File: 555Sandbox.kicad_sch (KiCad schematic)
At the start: 18 parts, among them J1 VIN, J2 Piezo, Q1 2N7000, SW1 RESET, U1 NE555P

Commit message: feat: update with separate freq and period adjustment
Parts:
- removed Q1: 2N7000, Package_TO_SOT_THT:TO-92_Inline, symbol Transistor_FET:2N7000
- added R7: 4K7, Resistor_THT:R_Axial_DIN0207_L6.3mm_D2.5mm_P7.62mm_Horizontal, symbol Device:R
- R6: value 10K -> 4K7
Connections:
- net GND: now also J2.1 (Pin_1), R5.2
- net OUT: now also D1.2 (A), J2.2 (Pin_2), U1.3 (Q); no longer J2.1 (Pin_1), R5.2
- net TRIG: now also RV1.2; no longer C3.1, RV1.3
- net VCC: now also R7.1; no longer D1.2 (A), J2.2 (Pin_2), R6.1
- net DIS: now reaches D12.2 (A), D13.1 (K)
- net DIS: now also U1.7 (DIS), R7.2; no longer U1.3 (Q)
- net VCAP: now reaches RV2.1, RV2.2
- net VCAP: now also C3.1; no longer D13.2 (A)
- net at D12.1 (K), RV1.1: no longer RV1.2
- net OSC_OUT: no longer names the net of R6.2
- net OSC_OUT: now also RV1.3; no longer U1.7 (DIS)
- new net: D13.2 (A), R6.1
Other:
- moved on the sheet: C3, D12, D13, RV1

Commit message: fix: connect trig to cap directly
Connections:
- net VCAP is gone; now on net TRIG: C3.1, RV2.1, RV2.2
- net TRIG: no longer RV1.2, RV2.3
- new net: RV1.2, RV2.3
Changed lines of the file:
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@@
 	)
 	(label "TRIG"
-		(at 139.7 113.03 180)
+		(at 151.13 116.84 0)
 		(fields_autoplaced yes)
 		(effects
@@
 				(size 1.27 1.27)
 			)
-			(justify right bottom)
+			(justify left bottom)
 		)
 	)

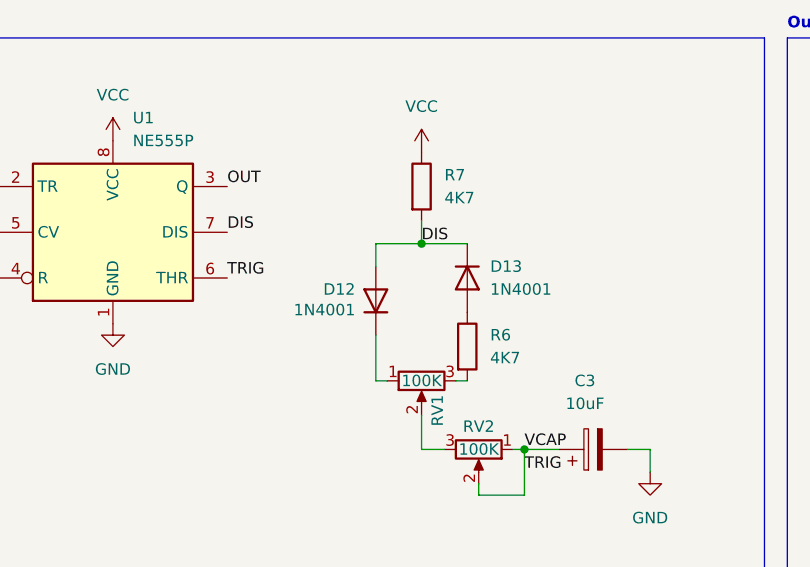
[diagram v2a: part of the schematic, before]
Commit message: fix: polarised capacitor and erronous silkscreen label
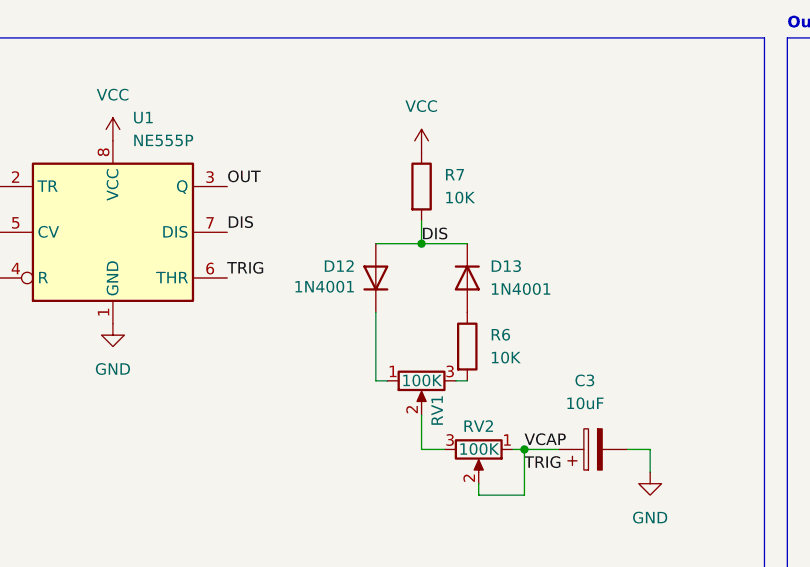
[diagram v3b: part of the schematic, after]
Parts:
- C3: footprint Capacitor_THT:C_Radial_D5.0mm_H11.0mm_P2.00mm -> Capacitor_THT:CP_Radial_D5.0mm_P2.00mm
- R6, R7: value 4K7 -> 10K
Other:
- moved on the sheet: D12
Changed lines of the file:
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@@
-	(wire
-		(pts
-			(xy 134.62 91.44) (xy 134.62 93.98)
-		)
-		(stroke
-			(width 0)
-			(type default)
-		)
-	)
 	(wire
 		(pts
@@
 	(wire
 		(pts
-			(xy 134.62 106.68) (xy 134.62 101.6)
+			(xy 134.62 106.68) (xy 134.62 99.06)
 		)
 		(stroke
@@
 			)
 		)
-		(property "Value" "4K7"
+		(property "Value" "10K"
 			(at 147.32 104.1399 0)
 			(effects
@@
 			)
 		)
-		(property "Footprint" "Capacitor_THT:C_Radial_D5.0mm_H11.0mm_P2.00mm"
+		(property "Footprint" "Capacitor_THT:CP_Radial_D5.0mm_P2.00mm"
 			(at 162.56 113.3348 0)
 			(effects
@@
 			)
 		)
-		(property "Value" "4K7"
+		(property "Value" "10K"
 			(at 142.24 86.3599 0)
 			(effects
@@
 	(symbol
 		(lib_id "Diode:1N4001")
-		(at 134.62 97.79 90)
+		(at 134.62 95.25 90)
 		(unit 1)
 		(exclude_from_sim no)
@@
 		(dnp no)
 		(property "Reference" "D12"
-			(at 132.334 96.52 90)
+			(at 132.334 93.98 90)
 			(effects
 				(font
@@
 		)
 		(property "Value" "1N4001"
-			(at 132.334 98.806 90)
+			(at 132.334 96.266 90)
 			(effects
 				(font
@@
 		)
 		(property "Footprint" "Diode_THT:D_DO-41_SOD81_P7.62mm_Horizontal"
-			(at 134.62 97.79 0)
+			(at 134.62 95.25 0)
 			(effects
 				(font
@@
 		)
 		(property "Datasheet" "http://www.vishay.com/docs/88503/1n4001.pdf"
-			(at 134.62 97.79 0)
+			(at 134.62 95.25 0)
 			(effects
 				(font
@@
 		)
 		(property "Description" "50V 1A General Purpose Rectifier Diode, DO-41"
-			(at 134.62 97.79 0)
+			(at 134.62 95.25 0)
 			(effects
 				(font
@@
 		)
 		(property "Sim.Device" "D"
-			(at 134.62 97.79 0)
+			(at 134.62 95.25 0)
 			(effects
 				(font
@@
 		)
 		(property "Sim.Pins" "1=K 2=A"
-			(at 134.62 97.79 0)
-			(effects
-				(font
+			(at 134.62 95.25 0)
+			(effects
+				(font

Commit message: feat: refresh majority of pcb to improve ease of assembly
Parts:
- removed H1, H2: MountingHole_Pad, MountingHole:MountingHole_2.7mm_M2.5_DIN965_Pad, symbol Mechanical:MountingHole_Pad
- removed J2: Piezo, Connector_PinHeader_2.54mm:PinHeader_1x02_P2.54mm_Vertical, symbol Connector:Conn_01x02_Pin
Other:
- moved on the sheet: D1, R5

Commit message: feat: board v1.4
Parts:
- removed D12, D13: 1N4001, Diode_THT:D_DO-41_SOD81_P7.62mm_Horizontal, symbol Diode:1N4001
- removed J1: VIN, Connector_Wire:SolderWire-1.5sqmm_1x02_P6mm_D1.7mm_OD3mm, symbol Connector:Conn_01x02_Pin
- removed R1: 10K, Resistor_THT:R_Axial_DIN0207_L6.3mm_D2.5mm_P7.62mm_Horizontal, symbol Device:R
- removed SW1: RESET, Button_Switch_THT:SW_PUSH_6mm_H4.3mm, symbol Switch:SW_Push
- removed U1: NE555P, Package_DIP:DIP-8_W7.62mm, symbol Timer:NE555P
- added BT1: Battery_Cell, Battery:BatteryHolder_Keystone_3000_1x12mm, symbol Device:Battery_Cell
- added D2, D3: 1N5819WS, Diode_SMD:D_SOD-323, symbol Diode:1N5819WS
- added H1: MountingHole_Pad, MountingHole:MountingHole_3mm_Pad, symbol Mechanical:MountingHole_Pad
- added SW1: SW_SPDT, Button_Switch_THT:SW_Slide_SPDT_Angled_CK_OS102011MA1Q, symbol Switch:SW_SPDT
- added U1: LMC555xM, Package_SO:SOIC-8_3.9x4.9mm_P1.27mm, symbol Timer:LMC555xM
- C1, C2: footprint Capacitor_THT:C_Disc_D4.7mm_W2.5mm_P5.00mm -> Capacitor_SMD:C_0603_1608Metric; Part (none) -> C14663
- C3: value 10uF -> 4.7uF; footprint Capacitor_THT:CP_Radial_D5.0mm_P2.00mm -> Capacitor_SMD:CP_Elec_5x5.4; Part (none) -> C336464
- D1: value OUT LED -> LED; footprint LED_THT:LED_D5.0mm -> LED_SMD:LED_PLCC_2835; Part (none) -> C7371920
- R5: value 200 -> 300; footprint Resistor_THT:R_Axial_DIN0207_L6.3mm_D2.5mm_P2.54mm_Vertical -> Resistor_SMD:R_0603_1608Metric; Part (none) -> C23025
- R6, R7: footprint Resistor_THT:R_Axial_DIN0207_L6.3mm_D2.5mm_P7.62mm_Horizontal -> Resistor_SMD:R_0603_1608Metric; Part (none) -> C25804
- RV1: value 100K -> 250K; footprint Potentiometer_THT:Potentiometer_Alps_RK163_Single_Horizontal -> Potentiometer_THT:Potentiometer_Runtron_RM-065_Vertical; now left out of the parts list
- RV2: value 100K -> 1M; footprint Potentiometer_THT:Potentiometer_Alps_RK163_Single_Horizontal -> Potentiometer_THT:Potentiometer_Runtron_RM-065_Vertical; now left out of the parts list
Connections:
- net DIS: now also D2.2 (A), D3.1 (K), U1.7 (DIS)
- net GND: now also BT1.2 (-), U1.1 (GND)
- net OUT: now also U1.3 (Q)
- net TRIG: now also U1.2 (TR), U1.6 (THR)
- net VCC: now also SW1.2 (B), U1.4 (R), U1.8 (VCC)
- net at R6.1: now also D3.2 (A)
- net at C2.1: now also U1.5 (CV)
- net at RV1.1: now also D2.1 (K)
- new net: BT1.1 (+), SW1.1 (A)
- no-connect marks 0 -> 2
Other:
- removed sheet Voltage Meter

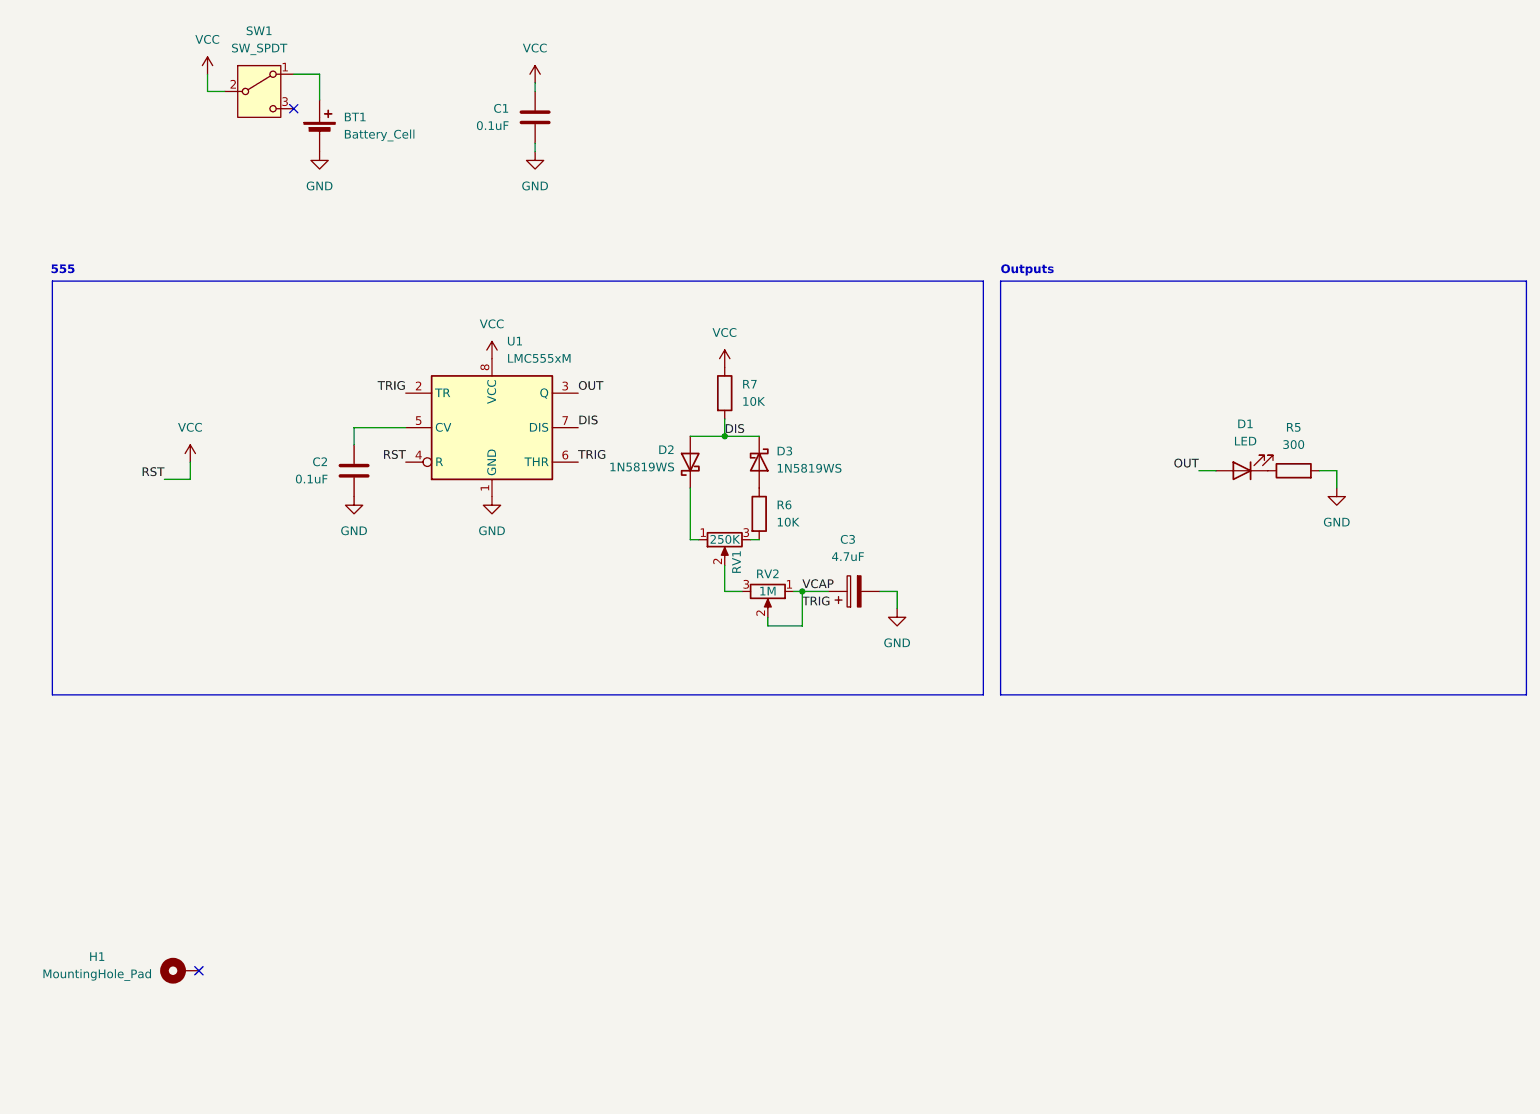
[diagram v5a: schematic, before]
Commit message: feat: microcontroller based v2.1
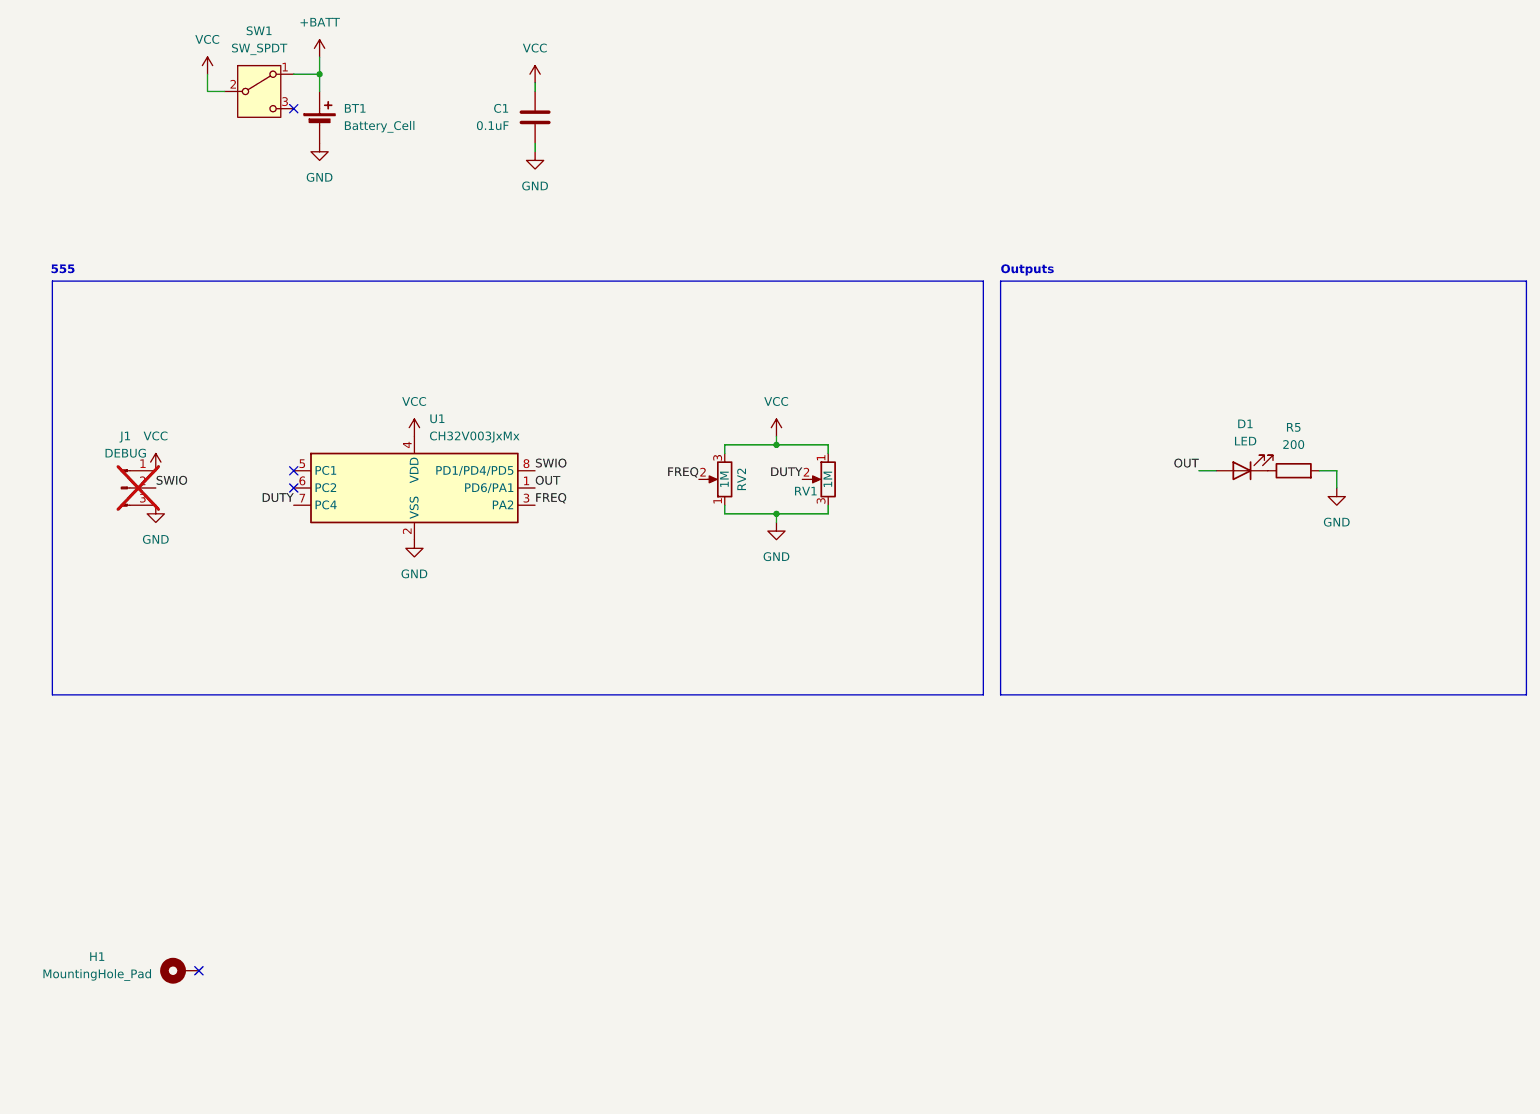
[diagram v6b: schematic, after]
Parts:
- removed C2: 0.1uF, Capacitor_SMD:C_0603_1608Metric, symbol Device:C
- removed C3: 4.7uF, Capacitor_SMD:CP_Elec_5x5.4, symbol Device:C_Polarized
- removed D2, D3: 1N5819WS, Diode_SMD:D_SOD-323, symbol Diode:1N5819WS
- removed R6, R7: 10K, Resistor_SMD:R_0603_1608Metric, symbol Device:R
- removed U1: LMC555xM, Package_SO:SOIC-8_3.9x4.9mm_P1.27mm, symbol Timer:LMC555xM
- added J1: DEBUG, Connector_PinHeader_1.27mm:PinHeader_1x03_P1.27mm_Vertical, symbol Connector:Conn_01x03_Pin
- added U1: CH32V003JxMx, Package_SO:SOP-8_3.9x4.9mm_P1.27mm, symbol MCU_WCH_CH32V0:CH32V003JxMx
- R5: value 300 -> 200; Part C23025 -> C8218
- RV1: value 250K -> 1M
- SW1: now left out of the parts list
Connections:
- net GND: now also RV1.3, RV2.1, J1.3 (Pin_3), U1.2 (VSS)
- net OUT: now also U1.1 (PD6/PA1)
- net VCC: now also RV1.1, RV2.3, J1.1 (Pin_1), U1.4 (VDD)
- net DUTY: now reaches RV1.2
- net DUTY: now also U1.7 (PC4); no longer RV2.3
- net +BATT: now reaches BT1.1 (+), SW1.1 (A)
- net TRIG renamed FREQ
- net FREQ: now also U1.3 (PA2); no longer RV2.1
- new net SWIO: J1.2 (Pin_2), U1.8 (PD1/PD4/PD5)
- no-connect marks 2 -> 4
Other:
- moved on the sheet: BT1, RV2
